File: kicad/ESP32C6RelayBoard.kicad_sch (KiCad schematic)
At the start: 117 parts, among them IC1 SPX1117M3-L-3-3_TR, J1 Screw_Terminal_01x02, J10 Screw_Terminal_01x03, J11 Screw_Terminal_01x03, J12 Screw_Terminal_01x03, J13 Screw_Terminal_01x03, J2 Conn_02x08_Odd_Even, J3 Screw_Terminal_01x02, J4 Screw_Terminal_01x02, J5 10118192-0001LF, J6 Screw_Terminal_01x02, J7 Screw_Terminal_01x02, J8 Screw_Terminal_01x03, J9 Screw_Terminal_01x03, K1 G5RL-K1-E-DC12, K2 G5RL-K1-E-DC12, K3 G5RL-K1-E-DC12, K4 G5RL-K1-E-DC12, Q1 FDN302P, U1 AP62300Z6-7, U10 INA232AIDDFR, U11 74HC237, U12 INA232AIDDFR, U13 FAN3241TMX, U14 FAN3241TMX, U2 ESP32-C6-MINI-1/U, U3 434133025816, U4 434133025816, U5 ESD401DPYR, U6 ESD401DPYR, U7 ESD401DPYR, U8 FAN3241TMX, U9 FAN3241TMX

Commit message: Initial version of PCB
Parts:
- removed D2: LED Orange, Resistor_SMD:R_0603_1608Metric, symbol Device:LED
- removed R4: 1k6, Resistor_SMD:R_0603_1608Metric, symbol Device:R
- added C40: 100nF/10V/10%, Capacitor_SMD:C_0201_0603Metric, symbol Device:C
- added D13: ESD5Z12T1G, Diode_SMD:D_SOD-523, symbol Diode:ESD5Zxx
- C32: value 0.22uF/100V -> 2.2uF/100V; footprint Capacitor_SMD:C_1206_3216Metric -> Capacitor_SMD:C_1210_3225Metric
- U8: footprint Onsemi:SOIC127P600X175-8N -> (none)
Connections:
- net +12V: now also D11.3 (K), D12.3 (K), D7.3 (K), D8.3 (K), K1.9 (S+/R+), K2.9 (S+/R+), K3.9 (S+/R+), K4.9 (S+/R+), D13.1 (K)
- net +3V3: now also C40.1
- net +5V: no longer J5.1, Q1.3 (D), U7.1 (A1)
- net CHIP_PU: now also J2.16 (Pin_16)
- net GND: now also C40.2, D13.2 (A); no longer J2.16 (Pin_16)
- net R1R: now also U9.4 (IN2); no longer U13.4 (IN2)
- net R1S: now also U9.3 (IN1); no longer U13.3 (IN1)
- net R2R: now also U13.4 (IN2); no longer U9.4 (IN2)
- net R2S: now also U13.3 (IN1); no longer U9.3 (IN1)
- net at K1.1 (R-), U8.5 (OUT2): now also D7.2 (A); no longer D7.1 (A)
- net at K1.8 (S-), U8.7 (OUT1): now also D7.1 (A); no longer D7.2 (A)
- net at K3.1 (R-), U13.5 (OUT2): now also D11.2 (A); no longer D11.1 (A)
- net at K3.8 (S-), U13.7 (OUT1): now also D11.1 (A); no longer D11.2 (A)
- net at K4.1 (R-), U14.5 (OUT2): now also D12.2 (A); no longer D12.1 (A)
- net at K4.8 (S-), U14.7 (OUT1): now also D12.1 (A); no longer D12.2 (A)
- net at K2.1 (R-), U9.5 (OUT2): now also D8.2 (A); no longer D8.1 (A)
- net at K2.8 (S-), U9.7 (OUT1): now also D8.1 (A); no longer D8.2 (A)
- new net +5V_USB: J5.1, Q1.3 (D), U7.1 (A1)
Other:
- moved on the sheet: C1, C25, C27, C37, C39, D11, D12, D7, D8, J3, R1

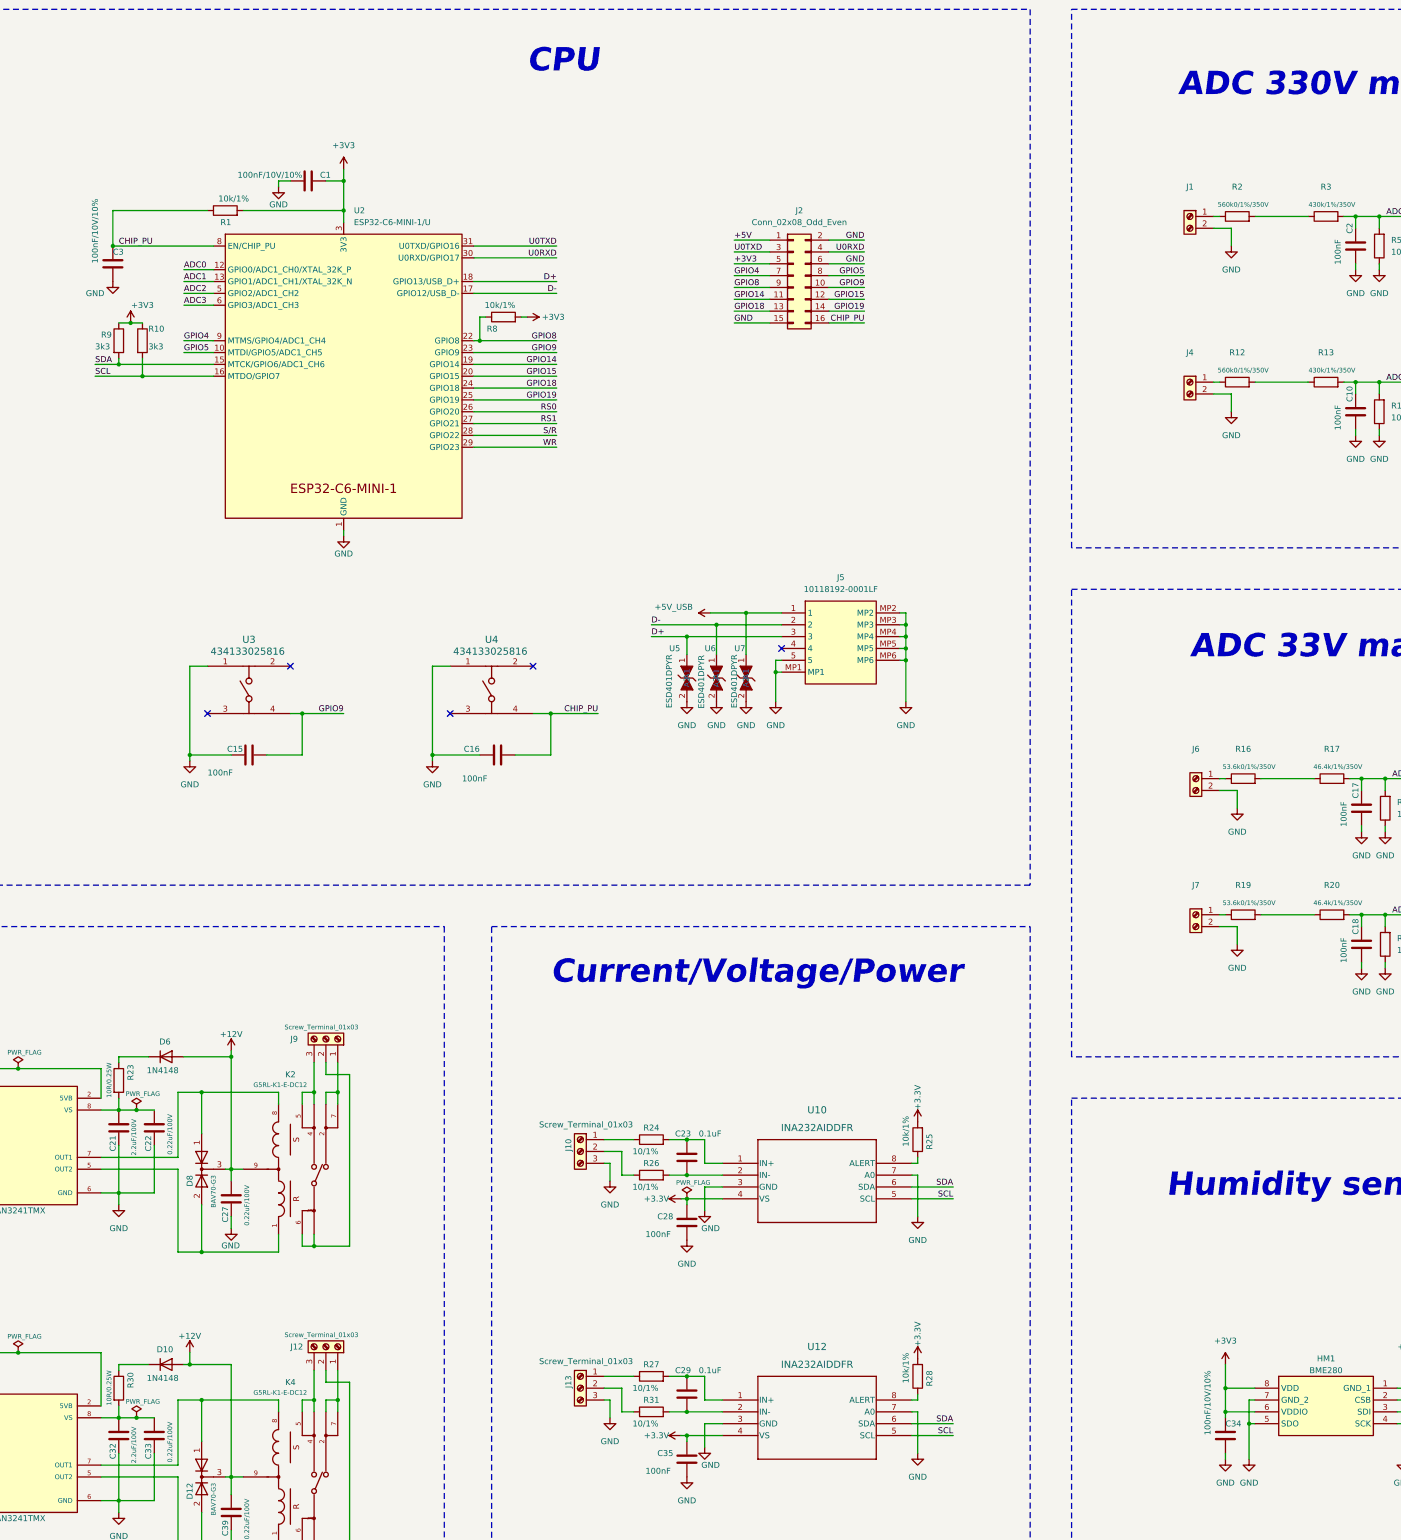
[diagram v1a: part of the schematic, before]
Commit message: Added LED
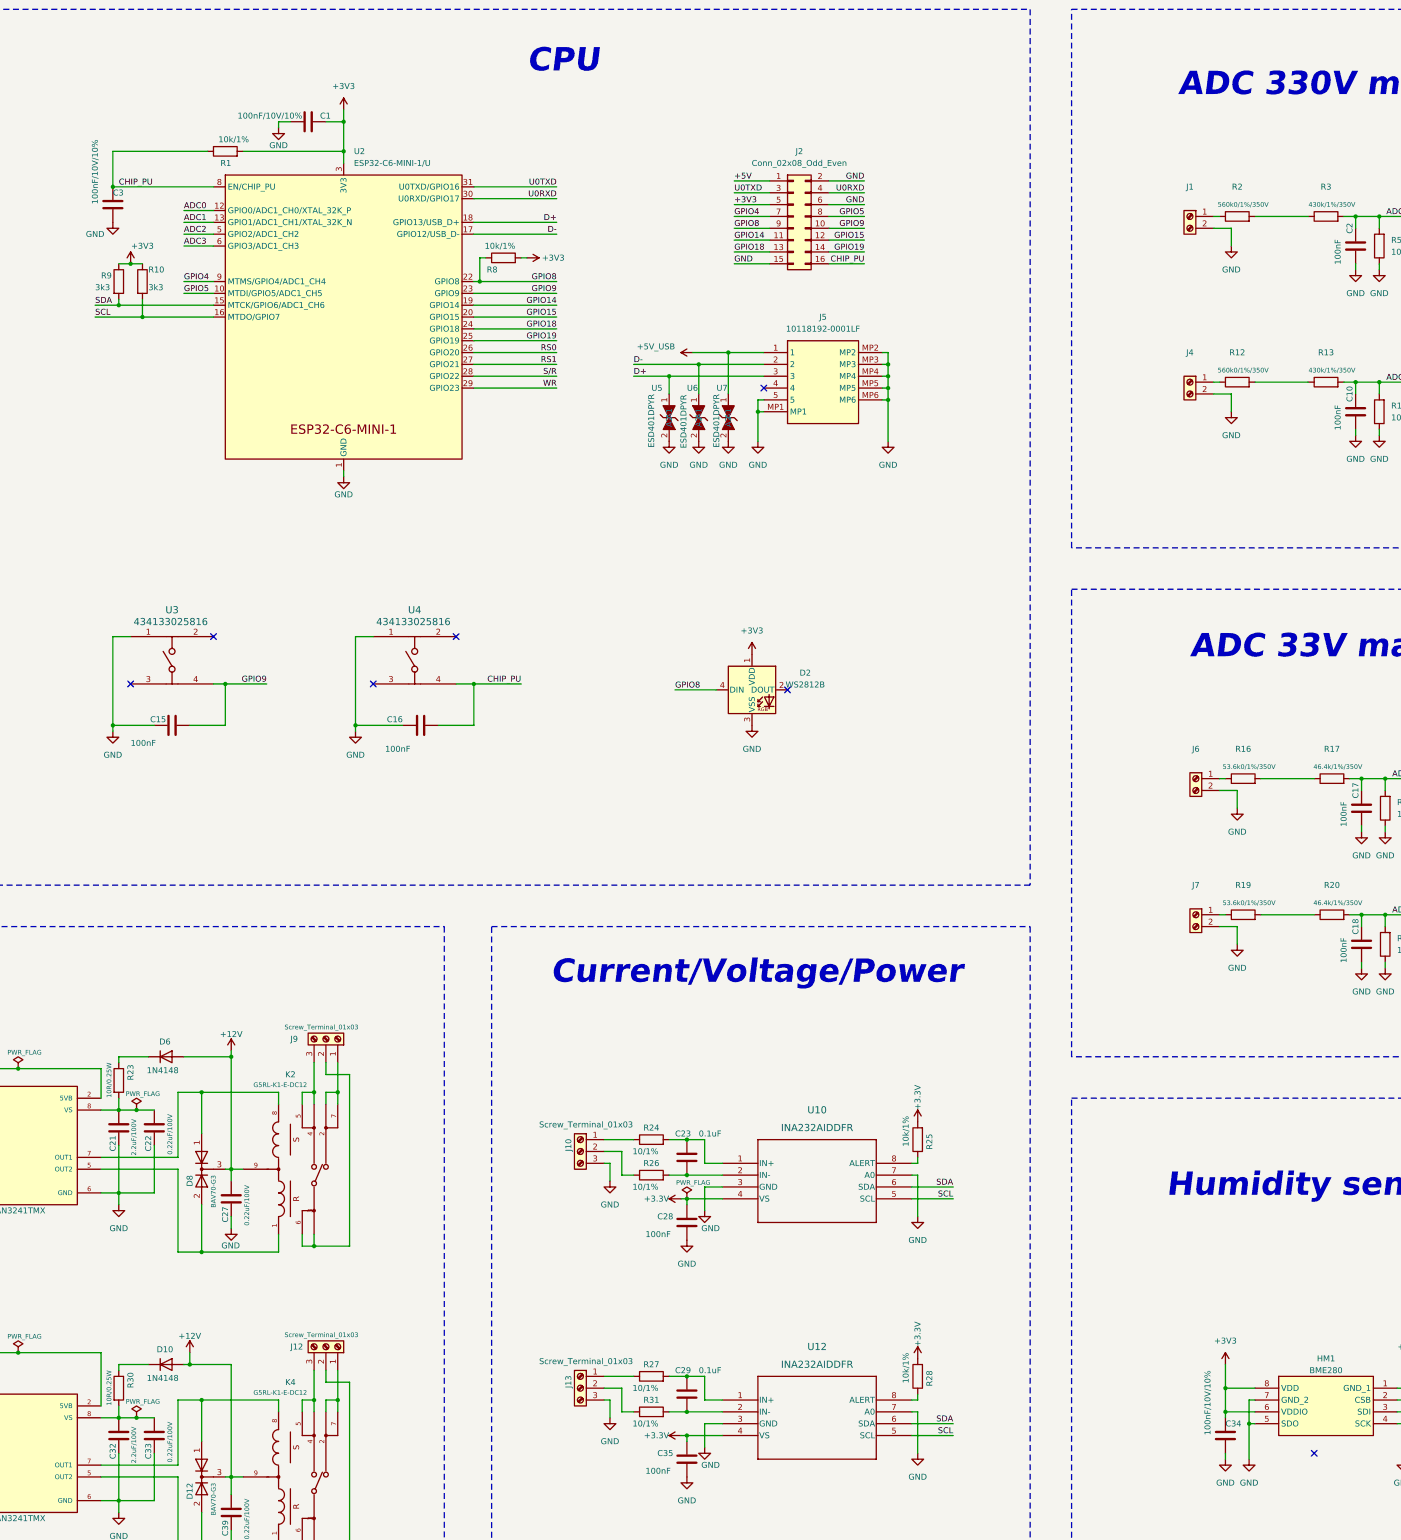
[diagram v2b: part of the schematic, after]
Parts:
- added D2: WS2812B, LED_SMD:LED_WS2812B_PLCC4_5.0x5.0mm_P3.2mm, symbol LED:WS2812B
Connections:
- net +3V3: now also D2.1 (VDD)
- net GND: now also D2.3 (VSS)
- net GPIO8: now also D2.4 (DIN)
- no-connect marks 6 -> 8
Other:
- moved on the sheet: C1, C15, C16, C3, J2, J5, R1, R10, R8, R9, U2, U3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
